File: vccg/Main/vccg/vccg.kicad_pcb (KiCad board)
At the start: 2 copper layers, 55.9 x 104.1 mm, 48 parts, among them J1 MelodyClock, J10 melody, J11 oled, J2 ChordClock, J3 ChordCV, J4 OctaveCV, J5 MelodyCV, J6 Conn_02x05_Odd_Even, J7 root, J8 chord1, J9 chord2, Q1 2N3904, Q2 2N3904, SW1 Key_Up, SW2 Key_down, SW3 is_minor, U1 MCP6004, U2 LM7805_TO220, U3 MCP4728, U4 TL074

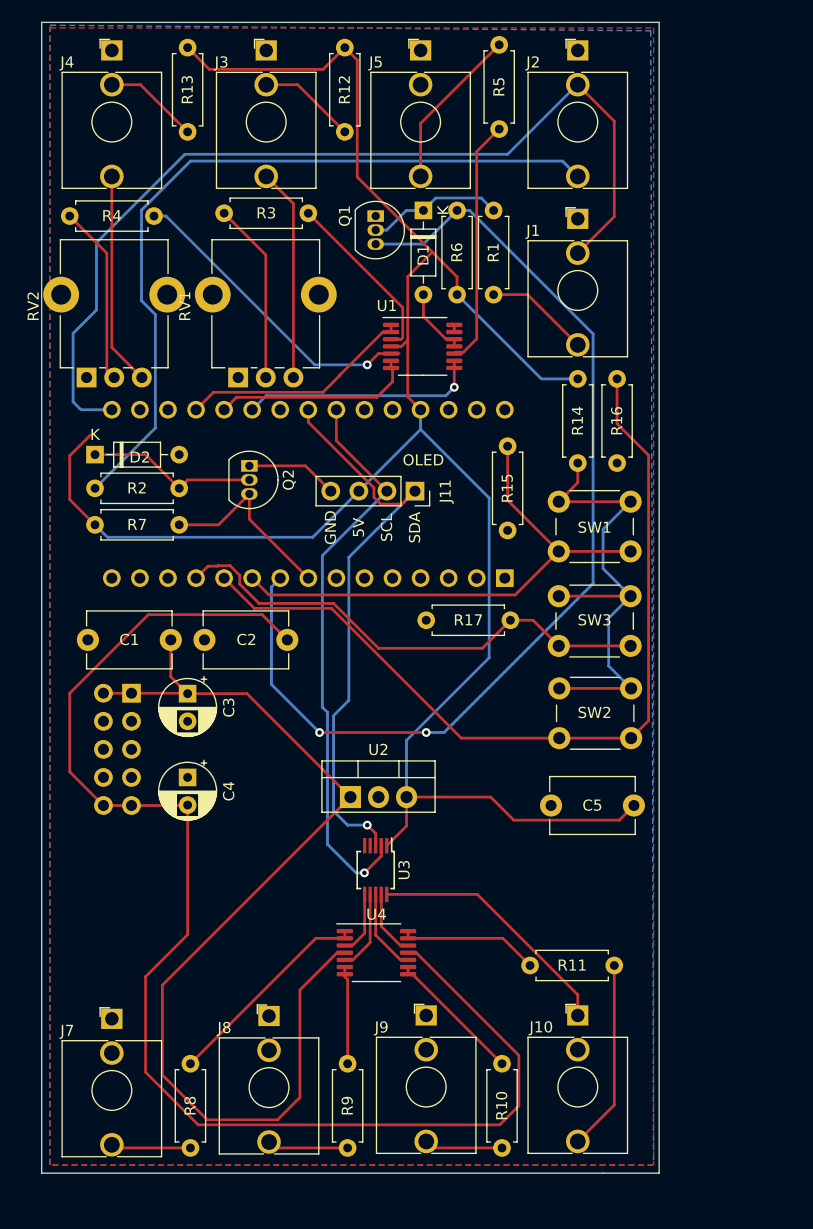
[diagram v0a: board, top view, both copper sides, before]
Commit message: add ic2 pull up resistors. Rewire to 10HP.
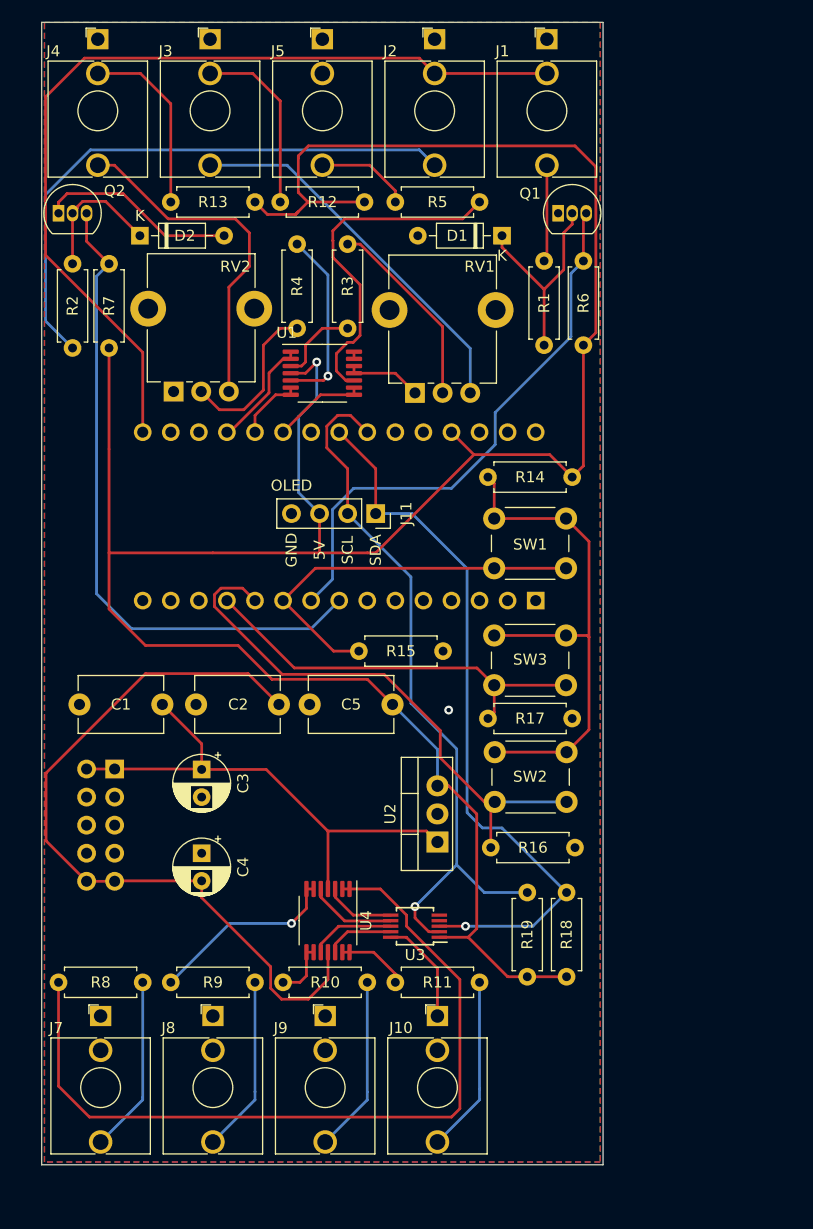
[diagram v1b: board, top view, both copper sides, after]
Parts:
- removed G***: LOGO, GrayNoise:13mmLogo
- added R18: 100K, Resistor_THT:R_Axial_DIN0207_L6.3mm_D2.5mm_P7.62mm_Horizontal, F.Cu at (225.3, 102.9)
- added R19: 100K, Resistor_THT:R_Axial_DIN0207_L6.3mm_D2.5mm_P7.62mm_Horizontal, F.Cu at (221.7, 102.9)
- moved R16 35.0 mm to (226.1, 98.8), turned to 180 degrees
- moved Q2 28.7 mm to (179.3, 41.4), turned to 0 degrees
- moved R7 24.5 mm to (183.9, 46.0), turned to 270 degrees
- moved C5 23.7 mm to (209.6, 85.9)
- moved R2 22.5 mm to (180.6, 46.0), turned to 270 degrees
- moved D2 20.2 mm to (186.7, 43.4)
- moved R10 19.3 mm to (207.3, 111.0), turned to 180 degrees
- moved R9 17.2 mm to (197.1, 111.0), turned to 180 degrees
- moved Q1 16.5 mm to (224.5, 41.4), turned to 0 degrees
- moved J1 16.5 mm to (223.5, 25.7)
- moved RV1 16.1 mm to (211.6, 57.7)
- moved R17 15.9 mm to (225.8, 87.1), turned to 180 degrees
- moved R8 15.6 mm to (186.9, 111.0), turned to 180 degrees
- moved R4 13.2 mm to (200.9, 44.2), turned to 270 degrees
- moved R1 13.0 mm to (223.3, 53.3), turned to 90 degrees
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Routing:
- net -12V: track 123.3 -> 68.8 mm
- net Net-(R8-Pad2): track 19.3 -> 73.5 mm
- net +5V: track 185.6 -> 234.6 mm, vias 0 -> 1
- net +12V: track 94.6 -> 48.6 mm
- net melodyClock: track 94.6 -> 50.5 mm, vias 2 -> 0
- net chordClock: track 17.3 -> 60.1 mm
- net key_down: track 77.2 -> 50.4 mm
- net Net-(J2-PadT): track 69.9 -> 52.3 mm
- net Net-(J3-PadT): track 19.2 -> 34.4 mm
- net SCL: track 51.4 -> 65.8 mm
- net SDA: track 52.6 -> 65.9 mm
- net melody: track 21.5 -> 8.47 mm, vias 1 -> 0
- net key_up: track 47.9 -> 35.6 mm
- net octave: track 18.2 -> 6.18 mm
- net Net-(J4-PadT): track 19.3 -> 31.4 mm
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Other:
- board size 55.9 x 104.1 mm -> 50.8 x 103.4 mm

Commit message: vccg updates and gbrs and stuff
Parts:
- removed R3, R4, R5: 100K, Resistor_THT:R_Axial_DIN0207_L6.3mm_D2.5mm_P7.62mm_Horizontal
- removed U4: TL074, Package_SO:TSSOP-14_4.4x5mm_P0.65mm
- C1, C2, C5: footprint Capacitor_THT:C_Disc_D7.5mm_W5.0mm_P7.50mm -> Capacitor_THT:C_Disc_D4.3mm_W1.9mm_P5.00mm
- moved C5 17.8 mm to (191.8, 84.7)
- moved R13 14.0 mm to (201.2, 48.0), turned to 90 degrees
- moved R12 9.62 mm to (205.2, 48.0), turned to 90 degrees
- moved C1 6.95 mm to (191.8, 79.6)
- moved C2 3.75 mm to (191.8, 82.1), turned to 180 degrees
- moved U3 1.87 mm to (213.4, 105.9)
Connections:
- R10 pad 2: Net-(R10-Pad2) -> chord2
- R11 pad 2: Net-(R11-Pad2) -> quant
- R8 pad 2: Net-(R8-Pad2) -> root
- R9 pad 2: Net-(R9-Pad2) -> chord1
- RV1 pad 2: Net-(R3-Pad2) -> Net-(RV1-Pad2)
- RV2 pad 2: Net-(R4-Pad2) -> Net-(RV2-Pad2)
- U1 pad 10: Net-(R5-Pad1) -> Net-(J5-PadT)
- U1 pad 3: Net-(R3-Pad1) -> Net-(RV1-Pad2)
- U1 pad 5: Net-(R4-Pad1) -> Net-(RV2-Pad2)
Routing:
- net Net-(R8-Pad2): track 73.5 -> 0.00 mm
- net +5V: track 234.6 -> 177.7 mm, vias 1 -> 0
- net -12V: track 68.8 -> 33.2 mm
- net Net-(R5-Pad1): track 31.2 -> 0.00 mm
- net root: track 6.44 -> 34.5 mm
- net GND: track 34.5 -> 8.78 mm
- net chord: track 10.2 -> 34.9 mm
- net Net-(R3-Pad2): track 17.7 -> 0.00 mm
- net Net-(R9-Pad2): track 17.5 -> 0.00 mm, vias 1 -> 0
- net Net-(R4-Pad1): track 16.6 -> 0.00 mm, vias 1 -> 0
- net Net-(RV1-Pad2): track 0.00 -> 16.3 mm
- net chord1: track 7.97 -> 24.1 mm
- net Net-(R4-Pad2): track 14.8 -> 0.00 mm
- net Net-(J5-PadT): track 8.58 -> 21.9 mm, vias 0 -> 1
- net SDA: track 65.9 -> 76.6 mm, vias 1 -> 0
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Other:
- board text added: "v0.2"
- board text removed: "v0.1"

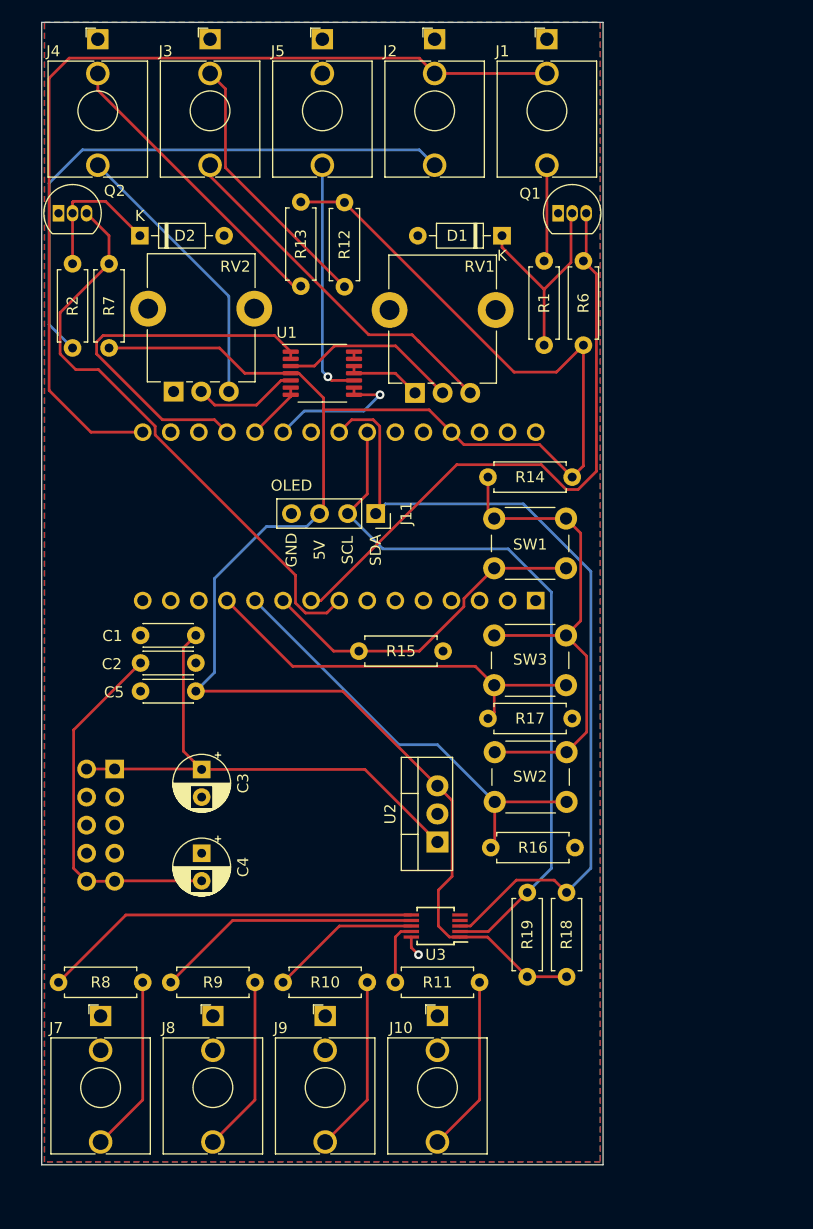
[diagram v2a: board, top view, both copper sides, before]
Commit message: updating to use pi pico, all parts on back
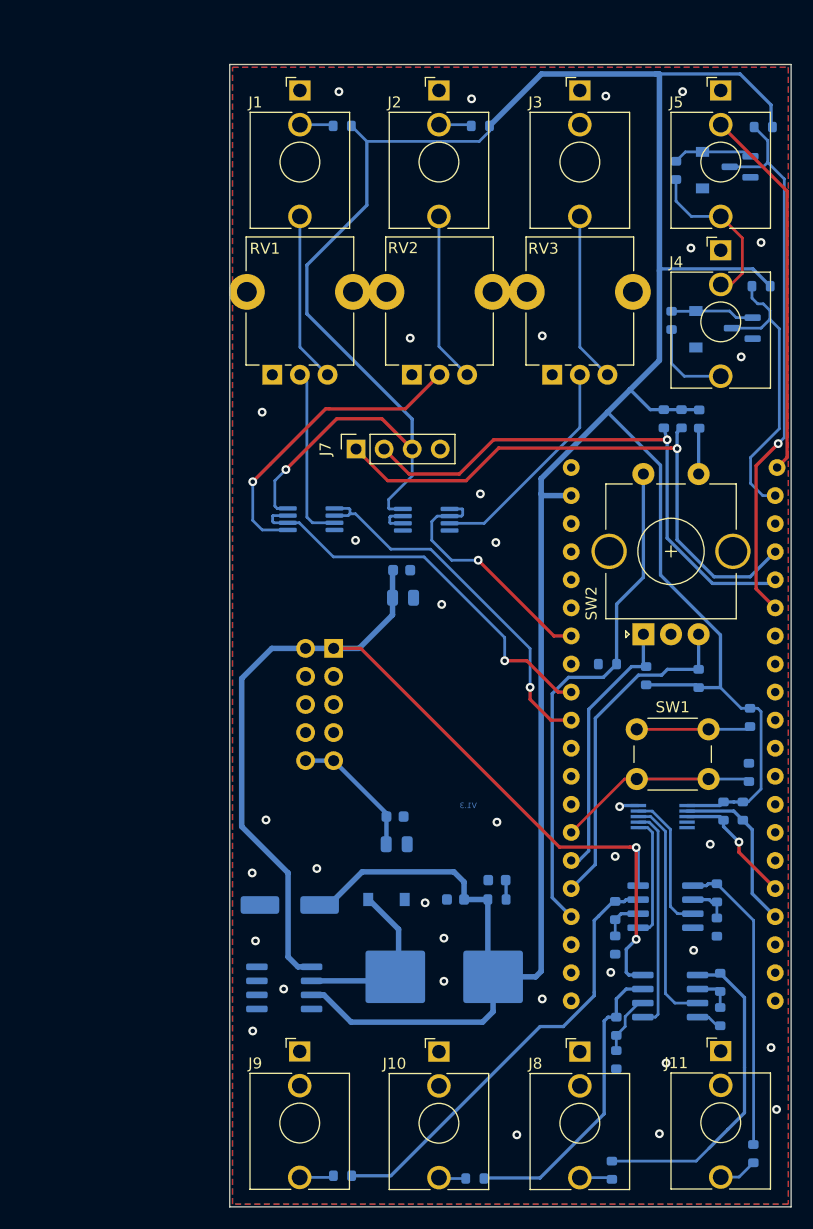
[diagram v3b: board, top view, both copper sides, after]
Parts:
- removed A1: Arduino_Nano_v3.x, Module:Arduino_Nano
- removed SW3: is_minor, Button_Switch_THT:SW_PUSH_6mm
- added C6: 220uF, Capacitor_SMD:CP_Elec_6.3x7.7, B.Cu at (200.2, 104.0)
- added D3: B5819W, Diode_SMD:D_SOD-123, B.Cu at (209.0, 103.5)
- added D4: LED, Diode_SMD:D_0603_1608Metric, B.Cu at (219.0, 101.8)
- added G***: LOGO, SynthStuff:GrayNoise15mm, B.Cu at (214.5, 86.6)
- added L1: 68uh 2A, SynthStuff:Inductor_SMD-L_SMMS1040, B.Cu at (214.2, 110.5)
- added M1: RaspberryPiPico, SynthStuff:Raspberry_Pi_Pico, B.Cu at (234.9, 88.4)
- added R20: 10K, Resistor_SMD:R_0603_1608Metric, B.Cu at (229.8, 115.0)
- added R21: 1K, Resistor_SMD:R_0603_1608Metric, B.Cu at (205.0, 128.5)
- added R22: 1K, Resistor_SMD:R_0603_1608Metric, B.Cu at (217.0, 128.8)
- added R23: 1K, Resistor_SMD:R_0603_1608Metric, B.Cu at (229.4, 128.0)
- added R24: 1K, Resistor_SMD:R_0603_1608Metric, B.Cu at (242.2, 126.5)
- added R25: 100K, Resistor_SMD:R_0603_1608Metric, B.Cu at (235.7, 60.0)
- added R26: 100K, Resistor_SMD:R_0603_1608Metric, B.Cu at (234.1, 60.0)
- added R27: 100K, Resistor_SMD:R_0603_1608Metric, B.Cu at (241.2, 95.5)
- added R28: 100K, Resistor_SMD:R_0603_1608Metric, B.Cu at (239.5, 95.5)
- added R29: 1K, Resistor_SMD:R_0603_1608Metric, B.Cu at (219.0, 103.5)
- added R3: 100K, Resistor_SMD:R_0603_1608Metric, B.Cu at (234.8, 51.1)
- added R4: 100K, Resistor_SMD:R_0603_1608Metric, B.Cu at (235.2, 37.5)
- added R5: 10K, Resistor_SMD:R_0603_1608Metric, B.Cu at (242.9, 48.0)
- added RV3: Melody, Potentiometer_THT:Potentiometer_Alpha_RD901F-40-00D_Single_Vertical_CircularHoles, F.Cu at (224.0, 56.0)
- added U4: MCP4728, Package_SO:MSOP-10_3x3mm_P0.5mm, B.Cu at (234.0, 96.0)
- added U5: LM2904, Package_SO:SOIC-8_3.9x4.9mm_P1.27mm, B.Cu at (234.2, 104.2)
- added U6: LM2904, Package_SO:SOIC-8_3.9x4.9mm_P1.27mm, B.Cu at (234.7, 112.2)
- C1, C2: footprint Capacitor_THT:C_Disc_D4.3mm_W1.9mm_P5.00mm -> Capacitor_SMD:C_0603_1608Metric; moved to B.Cu
- C3, C4: footprint Capacitor_THT:CP_Radial_D5.0mm_P2.50mm -> Capacitor_SMD:C_0805_2012Metric; moved to B.Cu
- C5: value 10n -> 100n; footprint Capacitor_THT:C_Disc_D4.3mm_W1.9mm_P5.00mm -> Capacitor_SMD:C_0603_1608Metric; moved to B.Cu
- D1, D2: footprint Diode_THT:D_DO-35_SOD27_P7.62mm_Horizontal -> Diode_SMD:D_SOD-123; moved to B.Cu
- J1: value MelodyClock -> ChordCV
- J10: value melody -> chord1
- J11: value oled -> melody; footprint Connector_PinSocket_2.54mm:PinSocket_1x04_P2.54mm_Vertical -> Connector_Audio:Jack_3.5mm_QingPu_WQP-PJ398SM_Vertical_CircularHoles
- J2: value ChordClock -> OctaveCV
- J3: value ChordCV -> MelodyCV
- J4: value OctaveCV -> MelodyClock
- J5: value MelodyCV -> ChordClock
- J7: value root -> oled; footprint Connector_Audio:Jack_3.5mm_QingPu_WQP-PJ398SM_Vertical_CircularHoles -> Connector_PinSocket_2.54mm:PinSocket_1x04_P2.54mm_Vertical
- J8: value chord1 -> chord2
- J9: value chord2 -> root
- Q1, Q2: value 2N3904 -> MMBT3904; footprint Package_TO_SOT_THT:TO-92_Inline -> Package_TO_SOT_SMD:SOT-23; moved to B.Cu
- R1, R2: value 100K -> 1K; footprint Resistor_THT:R_Axial_DIN0207_L6.3mm_D2.5mm_P7.62mm_Horizontal -> Resistor_SMD:R_0603_1608Metric; moved to B.Cu
- R10, R12, R8, R9: value 1K -> 100K; footprint Resistor_THT:R_Axial_DIN0207_L6.3mm_D2.5mm_P7.62mm_Horizontal -> Resistor_SMD:R_0603_1608Metric; moved to B.Cu
- R11, R14, R6: footprint Resistor_THT:R_Axial_DIN0207_L6.3mm_D2.5mm_P7.62mm_Horizontal -> Resistor_SMD:R_0603_1608Metric; moved to B.Cu
- R13: value 1K -> 10K; footprint Resistor_THT:R_Axial_DIN0207_L6.3mm_D2.5mm_P7.62mm_Horizontal -> Resistor_SMD:R_0603_1608Metric; moved to B.Cu
- R15, R16, R17, R18, R19: value 100K -> 10K; footprint Resistor_THT:R_Axial_DIN0207_L6.3mm_D2.5mm_P7.62mm_Horizontal -> Resistor_SMD:R_0603_1608Metric; moved to B.Cu
- R7: value 10K -> 1K; footprint Resistor_THT:R_Axial_DIN0207_L6.3mm_D2.5mm_P7.62mm_Horizontal -> Resistor_SMD:R_0603_1608Metric; moved to B.Cu
- SW1: value Key_Up -> Back; footprint Button_Switch_THT:SW_PUSH_6mm -> Button_Switch_THT:SW_PUSH_6mm_H13mm
- SW2: value Key_down -> RotaryEncoder_Switch; footprint Button_Switch_THT:SW_PUSH_6mm -> Rotary_Encoder:RotaryEncoder_Alps_EC11E-Switch_Vertical_H20mm_CircularMountingHoles
- U1: value MCP6004 -> MCP6002-xSN; footprint Package_SO:TSSOP-14_4.4x5mm_P0.65mm -> Package_SO:MSOP-8_3x3mm_P0.65mm; moved to B.Cu
- U2: value LM7805_TO220 -> MCP6002-xSN; footprint Package_TO_SOT_THT:TO-220-3_Vertical -> Package_SO:MSOP-8_3x3mm_P0.65mm; moved to B.Cu
- U3: value MCP4728 -> XL1509; footprint Package_SO:MSOP-10_3x3mm_P0.5mm -> Package_SO:SOIC-8_3.9x4.9mm_P1.27mm; moved to B.Cu
- moved R7 71.1 mm to (241.9, 87.0)
- moved R13 69.1 mm to (238.9, 106.0), turned to -90 degrees
- moved Q2 61.8 mm to (241.0, 37.2), turned to 180 degrees
- moved J4 59.5 mm to (239.2, 44.8)
- moved J11 57.8 mm to (239.2, 117.2), turned to 0 degrees
- moved J7 56.3 mm to (206.2, 62.7), turned to 90 degrees
- moved R11 54.7 mm to (237.3, 60.0), turned to -90 degrees
- moved R8 53.3 mm to (232.5, 83.2), turned to -90 degrees
- moved D2 51.3 mm to (237.6, 37.5), turned to -90 degrees
- moved R9 48.7 mm to (237.2, 83.5), turned to 90 degrees
- moved R14 43.9 mm to (229.7, 107.6), turned to -90 degrees
- moved R12 41.6 mm to (229.0, 82.2), turned to 180 degrees
- moved R15 41.5 mm to (239.2, 114.1), turned to -90 degrees
- moved R10 39.4 mm to (241.8, 92.0), turned to 90 degrees
- moved R2 39.0 mm to (217.5, 33.5), turned to 0 degrees
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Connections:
- C5 pad 1: +5V -> +3V3
- J1 pad TN: defaultClock -> Net-(J1-PadTN)
- J10 pad TN: (no net) -> unconnected-(J10-PadTN)
- J2 pad TN: defaultClock -> Net-(J2-PadTN)
- J3 pad TN: Net-(J3-PadTN) -> GND
- J5 pad T: Net-(J5-PadT) -> Net-(J4-PadTN)
- J5 pad TN: (no net) -> defaultClock
- J8 pad TN: (no net) -> unconnected-(J8-PadTN)
- J9 pad TN: (no net) -> unconnected-(J9-PadTN)
- Q1 pad 1: GND -> Net-(D1-Pad1)
- Q1 pad 2: Net-(D1-Pad1) -> GND
- Q2 pad 1: GND -> Net-(D2-Pad1)
- Q2 pad 2: Net-(D2-Pad1) -> GND
- R1 pad 1: Net-(D1-Pad1) -> Net-(J1-PadTN)
- R1 pad 2: Net-(J1-PadT) -> +3V3
- R10 pad 1: Net-(J9-PadT) -> back
- R10 pad 2: chord2 -> GND
- R11 pad 1: Net-(J10-PadT) -> +3V3
- R11 pad 2: quant -> Net-(R11-Pad2)
- R12 pad 1: Net-(J3-PadTN) -> select
- R12 pad 2: +5V -> GND
- R13 pad 1: Net-(J4-PadTN) -> Net-(R13-Pad1)
- R13 pad 2: +5V -> GND
- R14 pad 2: +5V -> GND
- R15 pad 1: GND -> Net-(R15-Pad1)
- R15 pad 2: key_up -> GND
- R16 pad 1: GND -> Net-(R16-Pad1)
- R16 pad 2: key_down -> GND
- R17 pad 1: GND -> Net-(R17-Pad1)
- R17 pad 2: is_minor -> Net-(R13-Pad1)
- R18 pad 1: SDA -> Net-(R18-Pad1)
- R18 pad 2: +5V -> Net-(R14-Pad1)
- R19 pad 1: SCL -> Net-(R19-Pad1)
- R19 pad 2: +5V -> Net-(R15-Pad1)
- R2 pad 1: Net-(D2-Pad1) -> Net-(J2-PadTN)
- R2 pad 2: Net-(J2-PadT) -> +3V3
- R6 pad 1: melodyClock -> chordClock
- R6 pad 2: +5V -> +3V3
- R7 pad 1: chordClock -> +3V3
- R7 pad 2: +5V -> Net-(R7-Pad2)
- R8 pad 1: Net-(J7-PadT) -> encoderA
- R8 pad 2: root -> +3V3
- R9 pad 1: Net-(J8-PadT) -> +3V3
- R9 pad 2: chord1 -> encoderB
- RV1 pad 3: Net-(J3-PadT) -> Net-(J1-PadT)
- RV2 pad 3: Net-(J4-PadT) -> Net-(J2-PadT)
- SW1 pad 1: Net-(R14-Pad1) -> Net-(R7-Pad2)
- SW1 pad 2: key_up -> back
- U1 pad 4: +5V -> GND
- U1 pad 8: melody -> +3V3
- U2 pad 1: +12V -> melody
- U2 pad 2: GND -> melody
- U2 pad 3: +5V -> Net-(RV3-Pad2)
- U3 pad 1: +5V -> +12V
- U3 pad 2: SCL -> Net-(D3-Pad1)
- U3 pad 3: SDA -> +3V3
- U3 pad 4: (no net) -> GND
- U3 pad 5: (no net) -> GND
- U3 pad 6: root -> GND
- U3 pad 7: chord1 -> GND
- U3 pad 8: chord2 -> GND
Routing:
- net +3V3: track 0.00 -> 318.4 mm, vias 0 -> 1
- net +5V: track 177.7 -> 0.00 mm
- net SDA: track 76.6 -> 0.00 mm
- net SCL: track 65.1 -> 0.00 mm
- net +12V: track 47.8 -> 101.2 mm, vias 0 -> 2
- net SDA1: track 0.00 -> 53.0 mm, vias 0 -> 1
- net defaultClock: track 84.7 -> 33.9 mm
- net SCL1: track 0.00 -> 49.5 mm, vias 0 -> 1
- net select: track 0.00 -> 46.0 mm
- net Net-(R14-Pad1): track 47.3 -> 3.77 mm
- net Net-(R18-Pad1): track 0.00 -> 40.3 mm
- net key_down: track 40.0 -> 0.00 mm
- net Net-(J2-PadT): track 52.5 -> 15.4 mm
- net is_minor: track 37.1 -> 0.00 mm
- net root: track 34.5 -> 0.00 mm
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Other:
- net class Default removed
- board text added: "Chord Quantizer"
- board text added: "V1.3"
- board text removed: "-12V"
- board text removed: "5V"
- board text removed: "GND"
- board text removed: "OLED"
- board text removed: "SCL"
- board text removed: "SDA"
- board text removed: "Voltage Controlled Chord Generator"
- board text removed: "v0.2"

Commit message: adding a diode to protect from usb5v.
rotating oled output pins to line up with oled module
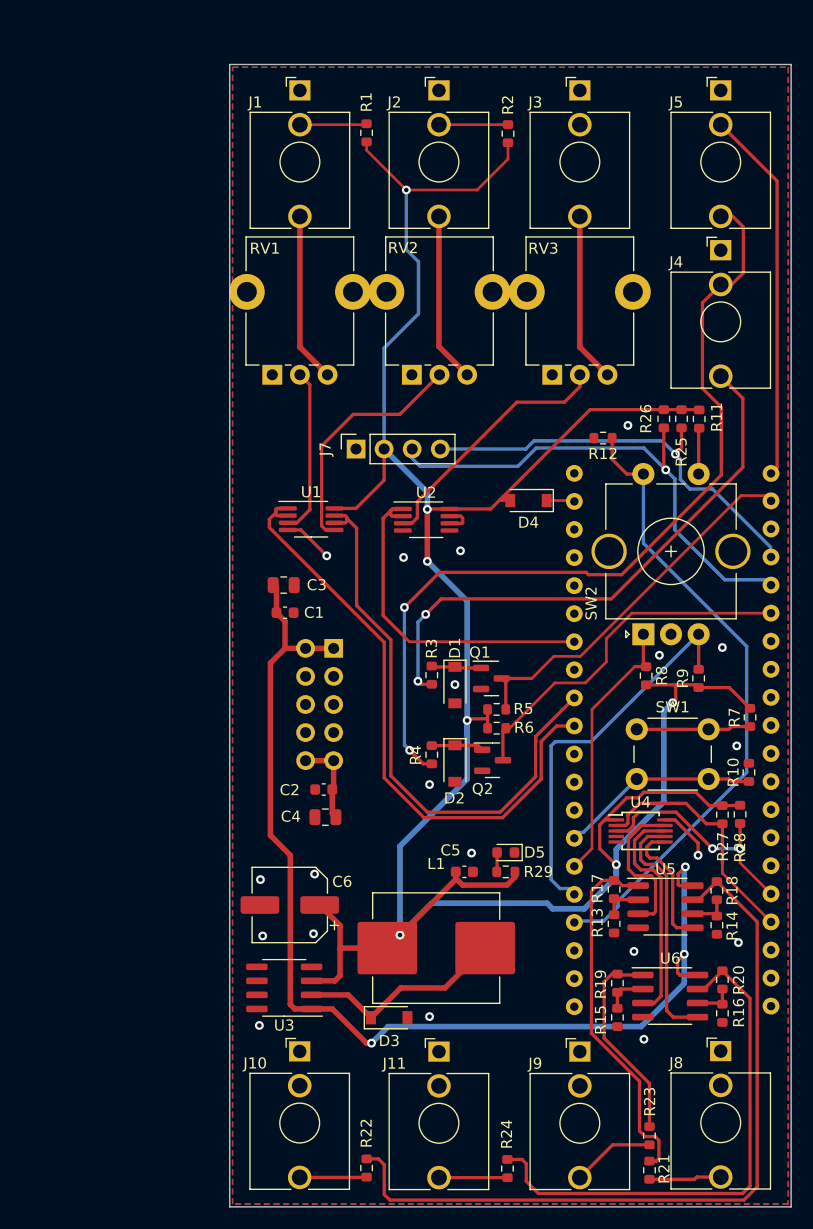
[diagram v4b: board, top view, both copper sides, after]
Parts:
- added D4: B5819W, Diode_SMD:D_SOD-123, F.Cu at (221.8, 67.4)
- C1, C2, C3, C4, C5, C6, D1, D2, D3, L1, Q1, Q2, R1, R10, R11, R12, R13, R14, R15, R16, R17, R18, R19, R2, R20, R23, R25, R26, R27, R28, R29, R3, R4, R5, R6, R7, R8, R9, U1, U2, U3, U4, U5, U6: moved to F.Cu
- D5: renamed from D4; moved to F.Cu
- R21: renamed from R24; moved to F.Cu
- R22: renamed from R21; moved to F.Cu
- R24: renamed from R22; moved to F.Cu
- moved R6 59.5 mm to (219.0, 88.0), turned to 180 degrees
- moved D2 58.2 mm to (215.2, 91.2)
- moved Q2 58.2 mm to (218.6, 90.9), turned to 0 degrees
- moved R4 57.3 mm to (213.1, 90.4)
- moved R5 45.2 mm to (219.0, 86.3), turned to 180 degrees
- moved Q1 39.0 mm to (218.5, 83.5), turned to 0 degrees
- moved D1 38.9 mm to (215.2, 84.1)
- moved R3 38.7 mm to (213.1, 83.2)
- moved R12 20.5 mm to (228.6, 61.8)
- moved C1 11.2 mm to (199.8, 77.5)
- moved C3 10.9 mm to (199.7, 75.0)
- moved D3 10.7 mm to (209.2, 114.2)
- moved R16 10.5 mm to (239.4, 113.8)
- moved R20 10.5 mm to (239.4, 110.8)
- moved R21 9.52 mm to (232.8, 128.0)
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- renumbered J9 to J10, J10 to J11, J11 to J8, J8 to J9
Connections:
- J7 pad 1: SDA1 -> GND
- J7 pad 2: SCL1 -> +3V3
- J7 pad 3: +3V3 -> SCL1
- J7 pad 4: GND -> SDA1
- M1 pad 39: +3V3 -> Net-(D4-Pad1)
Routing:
- net +3V3: track 318.4 -> 240.0 mm, vias 1 -> 7
- net Net-(J4-PadTN): track 14.9 -> 77.2 mm, vias 0 -> 2
- net Net-(J4-PadT): track 8.00 -> 51.0 mm, vias 0 -> 2
- net Net-(R18-Pad1): track 40.3 -> 71.0 mm
- net chord: track 33.8 -> 55.4 mm, vias 1 -> 0
- net Net-(R20-Pad1): track 27.4 -> 47.9 mm
- net chordClock: track 50.0 -> 32.6 mm, vias 1 -> 0
- net octave: track 36.5 -> 52.5 mm, vias 1 -> 0
- net SDA1: track 53.0 -> 38.8 mm
- net select: track 46.0 -> 57.7 mm
- net Net-(R19-Pad1): track 29.5 -> 18.6 mm
- net SDA0: track 11.6 -> 21.2 mm, vias 1 -> 2
- net melody: track 22.7 -> 30.8 mm, vias 1 -> 0
- net melodyClock: track 26.7 -> 34.4 mm
- net SCL0: track 15.3 -> 22.3 mm
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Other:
- board text added: "-12V Red Stripe"
- board text added: "v1.3"
- board text removed: "V1.3"
